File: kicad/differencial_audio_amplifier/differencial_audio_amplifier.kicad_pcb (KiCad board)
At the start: 2 copper layers, 30.1 x 19.8 mm, 35 parts, among them P1 CONN_01X03, P2 CONN_01X03, P3 CONN_01X03, U3 LM358

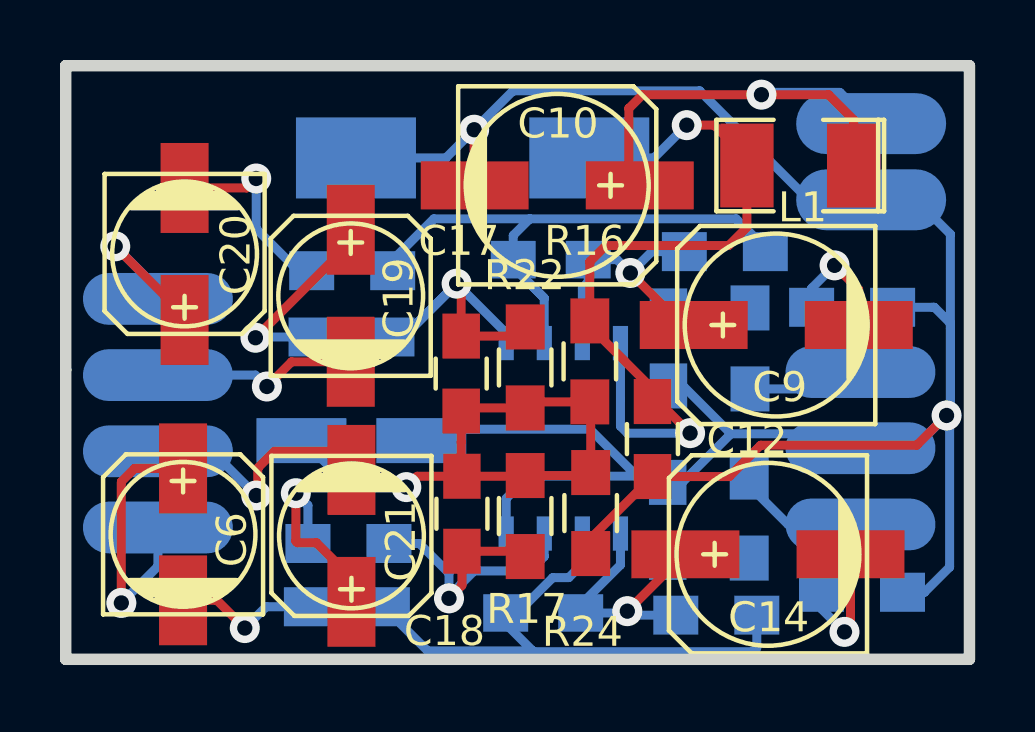
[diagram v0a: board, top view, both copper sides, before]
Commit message: change LM358 to ne5532, same pics from net with actual module, sold by elecfreeks
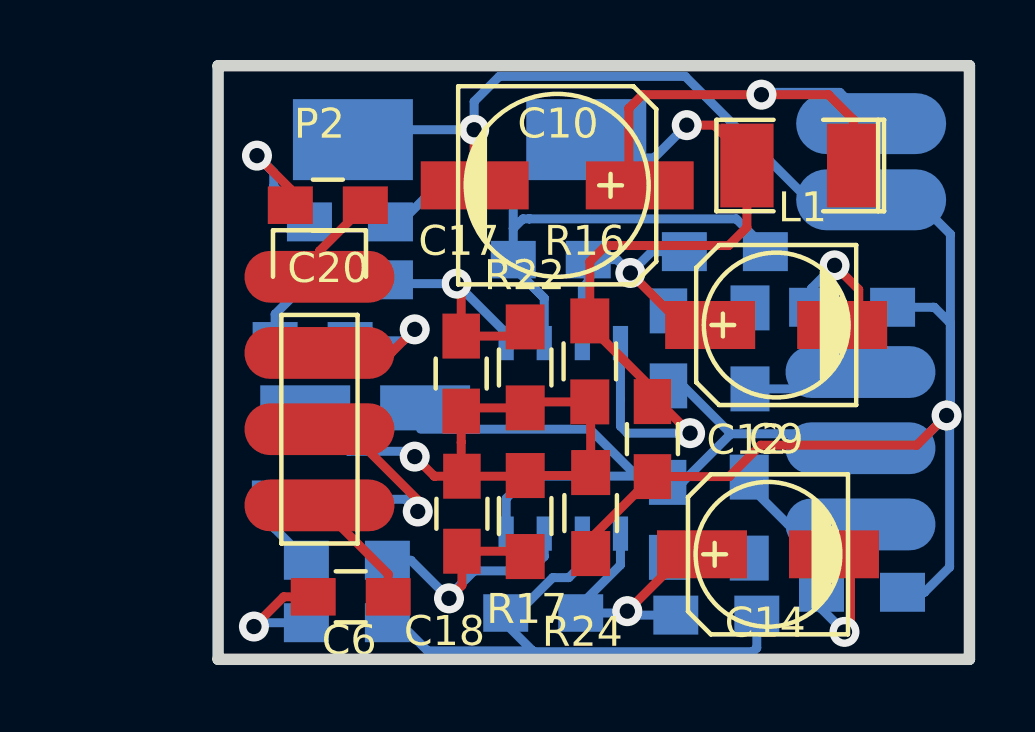
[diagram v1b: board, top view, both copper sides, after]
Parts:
- C13: value 2m2/16V -> 2u2/16V
- C14, C9: value 47m/25V -> 22m/16V; footprint Capacitors_SMD:c_elec_6.3x5.7 -> Capacitors_SMD:c_elec_5x5.3
- C19, C21: value 10m/16V -> 1u/16V; footprint Capacitors_SMD:c_elec_5x5.8 -> Capacitors_SMD:C_0805_HandSoldering; moved to B.Cu
- C20, C6: value 10m/16V -> 1u/16V; footprint Capacitors_SMD:c_elec_5x5.8 -> Capacitors_SMD:C_0805_HandSoldering
- P2: moved to F.Cu
- R10, R9: value 39R -> 4R7
- R11, R12: value 47k -> 100k
- R15, R18, R22, R24: value 47k -> 39k
- U3: value LM358 -> NE5532
- moved C6 5.96 mm to (104.7, 188.5), turned to 180 degrees
- moved P2 5.43 mm to (103.6, 177.9), turned to 0 degrees
- moved C20 5.04 mm to (103.9, 175.5), turned to 180 degrees
- moved C19 1.96 mm to (103.4, 180.0), turned to 0 degrees
- moved R20 1.91 mm to (104.6, 178.0)
- moved C21 1.80 mm to (103.4, 185.3), turned to 0 degrees
- moved R21 1.63 mm to (104.6, 176.0)
- moved C13 1.10 mm to (105.2, 182.2)
- moved C11 0.62 mm to (108.6, 173.3)
- moved R23 0.56 mm to (104.5, 187.3)
- moved R8 0.53 mm to (104.5, 189.4)
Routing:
- net /BTOUTR-: track 11.8 -> 5.81 mm
- net /BTOUTL+: track 9.30 -> 4.00 mm, vias 1 -> 0
- net Net-(C19-Pad1): track 6.77 -> 2.51 mm, vias 1 -> 0
- net Net-(C21-Pad1): track 6.61 -> 2.47 mm, vias 1 -> 0
- net Net-(C17-Pad1): track 12.4 -> 9.38 mm
- net GNDA: track 88.4 -> 91.2 mm
- net /BTOUTR+: track 5.75 -> 3.02 mm, vias 1 -> 0
- net /BTOUTL-: track 9.04 -> 7.19 mm
- net Net-(C20-Pad2): track 6.62 -> 5.05 mm
- net Net-(C18-Pad1): track 12.1 -> 11.4 mm
- net Net-(C6-Pad2): track 4.79 -> 4.19 mm
- net Net-(C15-Pad2): track 20.2 -> 20.7 mm
- net /VGND: track 20.0 -> 19.5 mm
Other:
- board size 30.1 x 19.8 mm -> 25 x 19.8 mm
